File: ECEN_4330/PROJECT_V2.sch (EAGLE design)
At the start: 30 parts, among them IC1 74AS573N

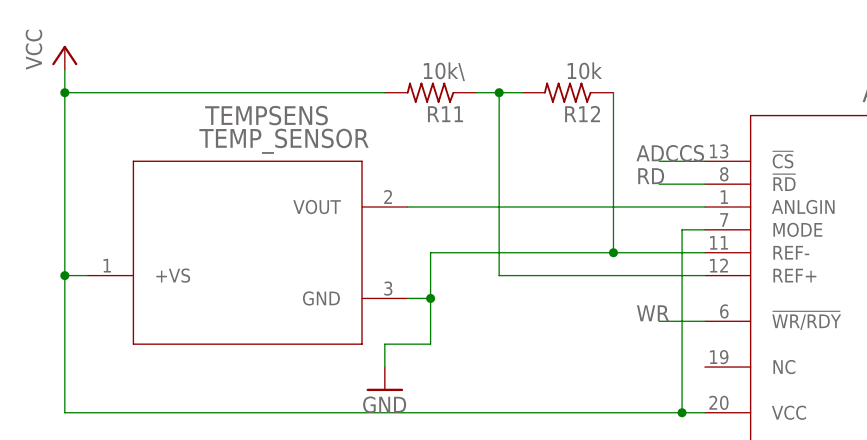
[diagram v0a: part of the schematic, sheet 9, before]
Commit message: Added Color select interfacing
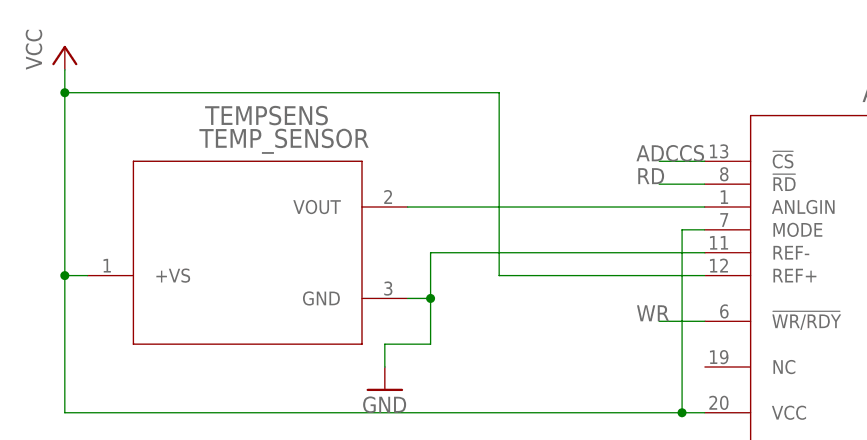
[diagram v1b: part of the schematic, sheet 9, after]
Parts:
- removed R11: 10k\, rcl:R-US_0204/5
- removed R12: 10k, rcl:R-US_0204/5
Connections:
- removed net N$30: ADC.REF+, R11.1, R12.2
- net GND: no longer R12.1
- net P3.5: now also CSLOGICG$1.I6
- net VCC: now also ADC.REF+; no longer R11.2
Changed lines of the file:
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@@
 <part name="GND8" library="supply1" library_urn="urn:adsk.eagle:library:371" deviceset="GND" device=""/>
 <part name="P+10" library="supply1" library_urn="urn:adsk.eagle:library:371" deviceset="VCC" device=""/>
-<part name="R11" library="rcl" library_urn="urn:adsk.eagle:library:334" deviceset="R-US_" device="0204/5" package3d_urn="urn:adsk.eagle:package:23488/1" value="10k\"/>
-<part name="R12" library="rcl" library_urn="urn:adsk.eagle:library:334" deviceset="R-US_" device="0204/5" package3d_urn="urn:adsk.eagle:package:23488/1" value="10k"/>
 <part name="GND9" library="supply1" library_urn="urn:adsk.eagle:library:371" deviceset="GND" device=""/>
 <part name="IC1" library="Fuckboiz" deviceset="74*573" device="N" technology="AS"/>
@@
 </segment>
 </net>
+<net name="COLORCS" class="0">
+<segment>
+<pinref part="CSLOGIC" gate="G$1" pin="O6"/>
+<wire x1="43.18" y1="162.56" x2="48.26" y2="162.56" width="0.1524" layer="91"/>
+<label x="45.72" y="162.56" size="1.778" layer="95"/>
+</segment>
+</net>
 <net name="WR" class="0">
 <segment>
@@
 </segment>
 </net>
-<net name="COLORCS" class="0">
-<segment>
-<pinref part="CSLOGIC" gate="G$1" pin="O6"/>
-<wire x1="43.18" y1="162.56" x2="48.26" y2="162.56" width="0.1524" layer="91"/>
-<label x="45.72" y="162.56" size="1.778" layer="95"/>
+<net name="P3.5" class="0">
+<segment>
+<pinref part="CSLOGIC" gate="G$1" pin="I6"/>
+<wire x1="17.78" y1="154.94" x2="12.7" y2="154.94" width="0.1524" layer="91"/>
+<label x="10.16" y="154.94" size="1.778" layer="95"/>
 </segment>
 </net>
@@
 <instance part="GND8" gate="1" x="132.08" y="106.68"/>
 <instance part="P+10" gate="VCC" x="10.16" y="157.48"/>
-<instance part="R11" gate="G$1" x="50.8" y="152.4" rot="R180"/>
-<instance part="R12" gate="G$1" x="66.04" y="152.4" rot="R180"/>
 <instance part="GND9" gate="1" x="45.72" y="119.38"/>
 </instances>
@@
 <wire x1="50.8" y1="124.46" x2="45.72" y2="124.46" width="0.1524" layer="91"/>
 <pinref part="ADC" gate="A" pin="REF-"/>
-<wire x1="81.28" y1="134.62" x2="71.12" y2="134.62" width="0.1524" layer="91"/>
-<wire x1="71.12" y1="134.62" x2="50.8" y2="134.62" width="0.1524" layer="91"/>
+<wire x1="81.28" y1="134.62" x2="50.8" y2="134.62" width="0.1524" layer="91"/>
 <wire x1="50.8" y1="134.62" x2="50.8" y2="129.54" width="0.1524" layer="91"/>
 <junction x="50.8" y="129.54"/>
-<pinref part="R12" gate="G$1" pin="1"/>
-<wire x1="71.12" y1="152.4" x2="71.12" y2="134.62" width="0.1524" layer="91"/>
-<junction x="71.12" y="134.62"/>
 <pinref part="GND9" gate="1" pin="GND"/>
 <wire x1="45.72" y1="124.46" x2="45.72" y2="121.92" width="0.1524" layer="91"/>
@@
 </segment>
 </net>
-<net name="N$30" class="0">
-<segment>
-<pinref part="R11" gate="G$1" pin="1"/>
-<pinref part="R12" gate="G$1" pin="2"/>
-<wire x1="55.88" y1="152.4" x2="58.42" y2="152.4" width="0.1524" layer="91"/>
-<pinref part="ADC" gate="A" pin="REF+"/>
-<wire x1="58.42" y1="152.4" x2="60.96" y2="152.4" width="0.1524" layer="91"/>
-<wire x1="81.28" y1="132.08" x2="58.42" y2="132.08" width="0.1524" layer="91"/>
-<wire x1="58.42" y1="132.08" x2="58.42" y2="152.4" width="0.1524" layer="91"/>
-<junction x="58.42" y="152.4"/>
-</segment>
-</net>
 <net name="VCC" class="0">
 <segment>
@@
 <wire x1="12.7" y1="132.08" x2="10.16" y2="132.08" width="0.1524" layer="91"/>
 <wire x1="10.16" y1="132.08" x2="10.16" y2="152.4" width="0.1524" layer="91"/>
-<pinref part="R11" gate="G$1" pin="2"/>
-<wire x1="10.16" y1="152.4" x2="45.72" y2="152.4" width="0.1524" layer="91"/>
+<wire x1="10.16" y1="152.4" x2="58.42" y2="152.4" width="0.1524" layer="91"/>
 <wire x1="10.16" y1="152.4" x2="10.16" y2="154.94" width="0.1524" layer="91"/>
 <junction x="10.16" y="152.4"/>
@@
 <wire x1="10.16" y1="116.84" x2="10.16" y2="132.08" width="0.1524" layer="91"/>
 <junction x="10.16" y="132.08"/>
-</segment>
-</net>
+<pinref part="ADC" gate="A" pin="REF+"/>
+<wire x1="81.28" y1="132.08" x2="58.42" y2="132.08" width="0.1524" layer="91"/>
+<wire x1="58.42" y1="132.08" x2="58.42" y2="152.4" width="0.1524" layer="91"/>
+</segment>
+</net>

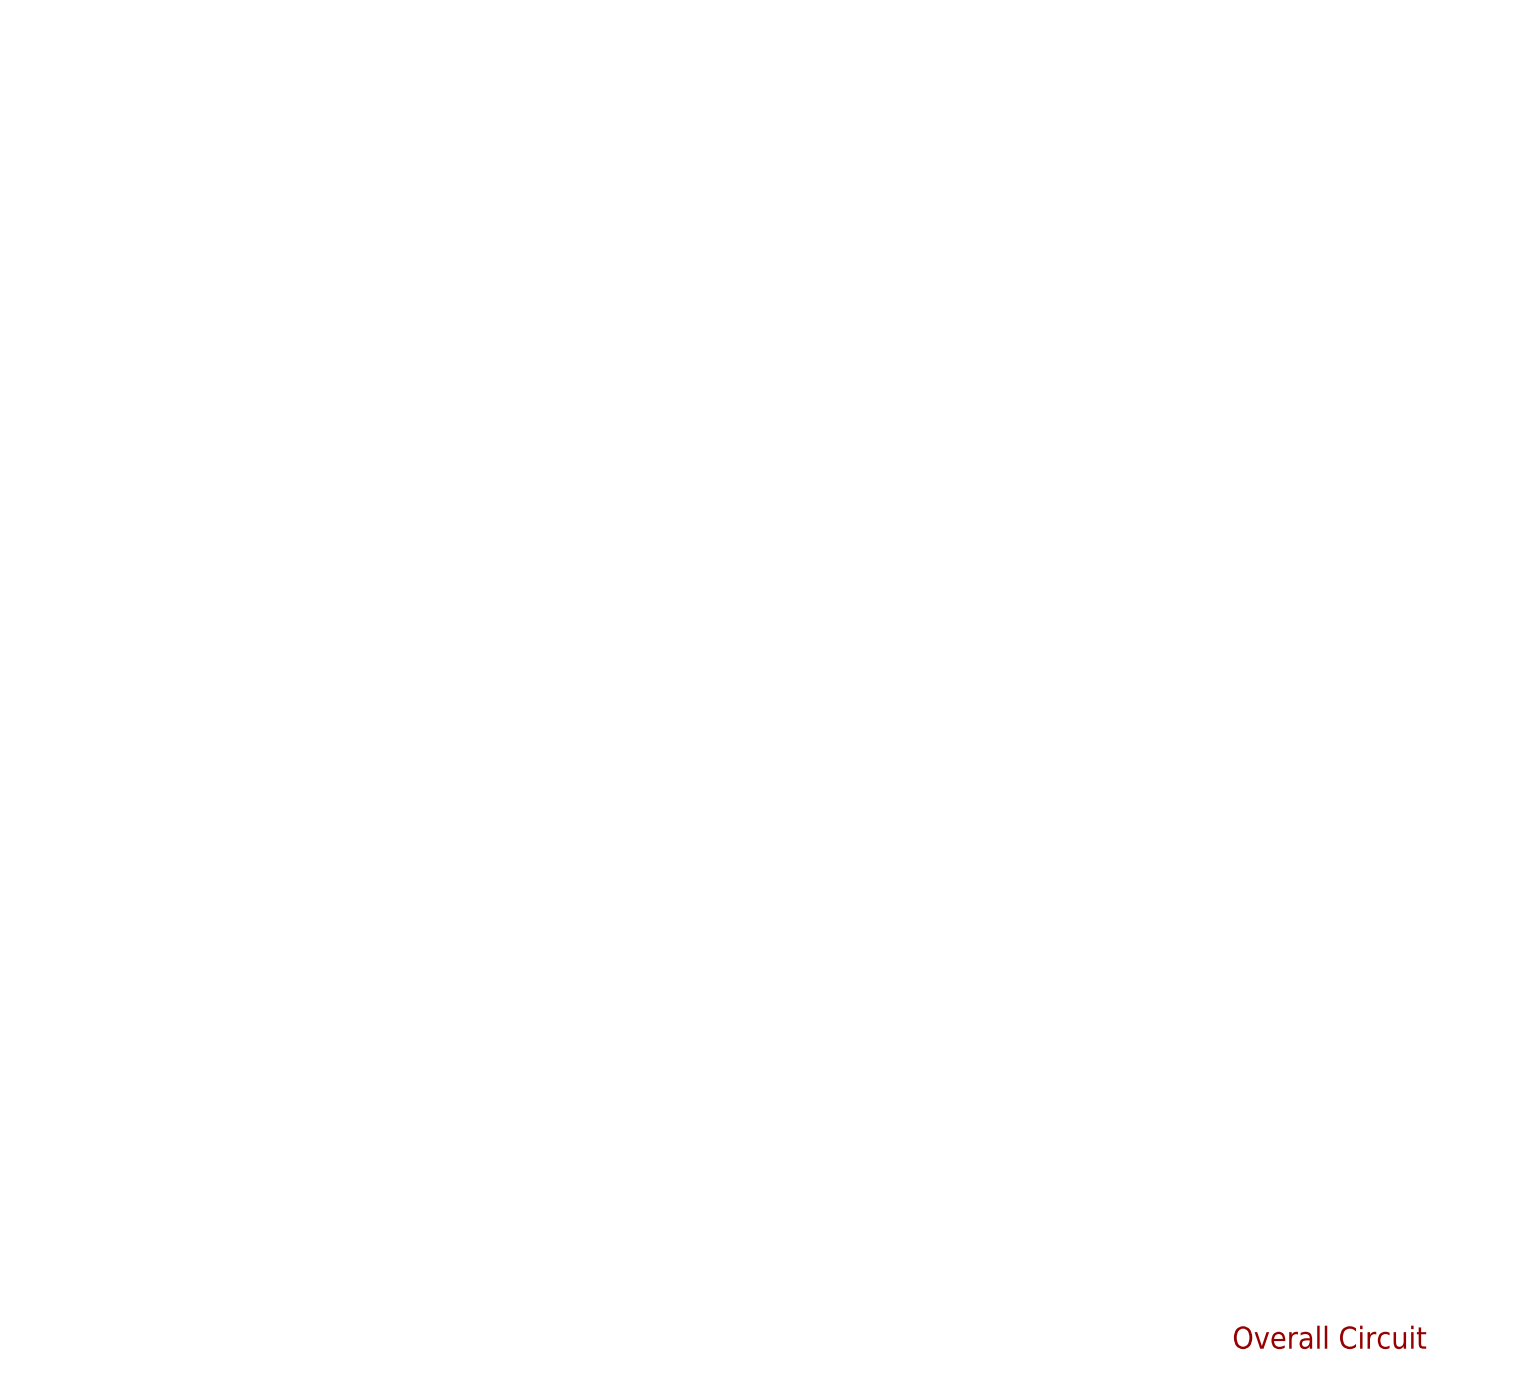
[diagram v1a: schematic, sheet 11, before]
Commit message: Started adding power circuit, changed switch to match footprint, started debugging RTC bug
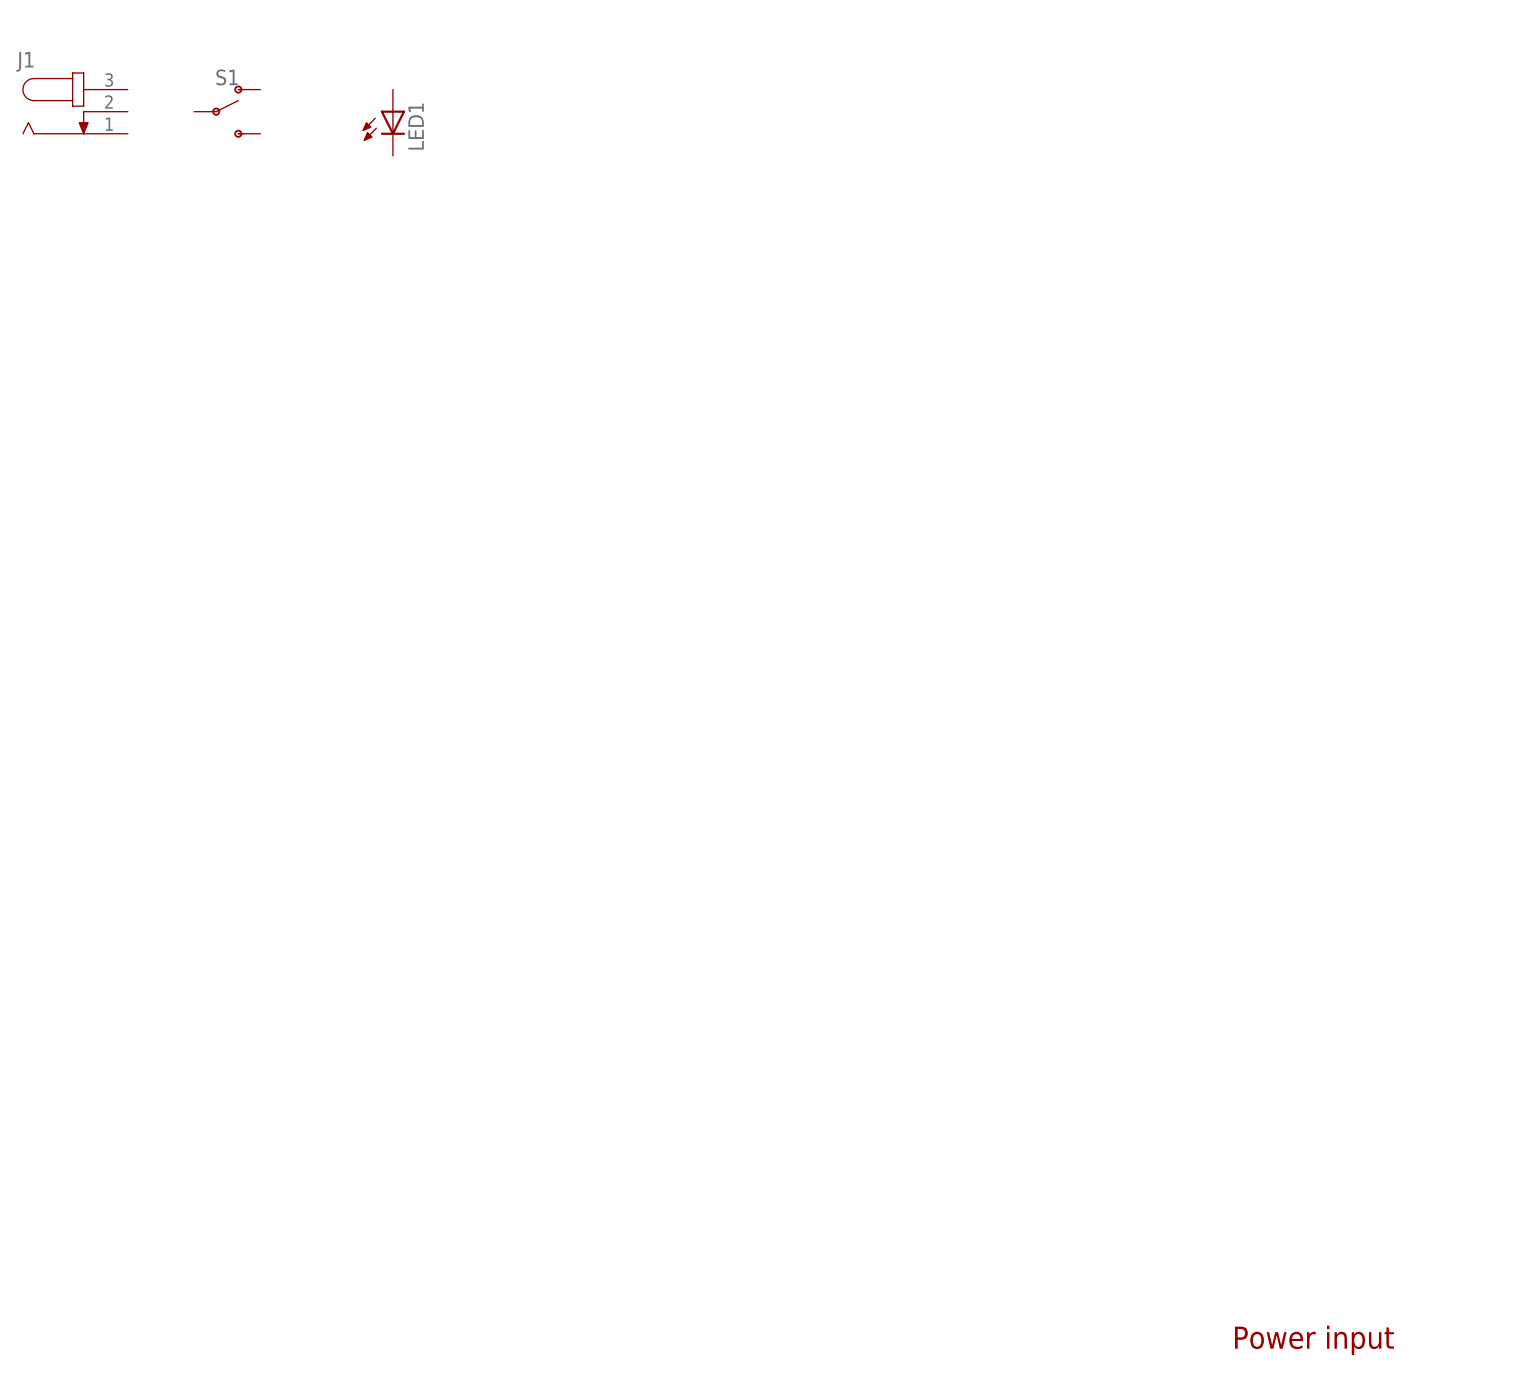
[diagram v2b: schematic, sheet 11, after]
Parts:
- removed RSTSW: (no value), adafruit:SWITCH_PUSHBUTTONEVQ-PE
- added J1: (no value), Fuckboiz:JACK-PLUG0
- added LED1: (no value), adafruit:LED5MM
- added RSTSWITCH: MOMENTARY-SWITCH-SPST-PTH-6.0MM, SparkFun-Switches:MOMENTARY-SWITCH-SPST-PTH-6.0MM
- added S1: (no value), Fuckboiz:SPDT_SWITCH-PTH-11.6X4.0MM-LOCK
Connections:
- net N$15: now also RSTSWITCH.1; no longer RSTSW.P$1
- net VCC: now also RSTSWITCH.2; no longer RSTSW.P$2
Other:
- note added: "Power input"
- note removed: "Overall Circuit"

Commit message: Final design before hierarchiel block
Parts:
- added R11: (no value), resistor:R-US_0204/7
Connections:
- new net N$30: J1.3, LED1.A, S1.S
- new net N$48: S1.O
- new net N$49: LED1.C, R11.2
- net GND: now also J1.1, J1.2, R11.1
- net VCC: now also S1.P
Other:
- moved on the sheet: J1, LED1, RAM1, RAM2, RTC, S1

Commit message: Added hierarchy sheet
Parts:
- removed 7SEG: 7_SEG, Fuckboiz:7_SEG
- removed 7SEGLATCH: 74HC573N, Fuckboiz:74HC573N
- removed ADC: ADC, Fuckboiz:ADC
- removed C1: 10u, adafruit:C-US025-025X050
- removed CLK: (no value), crystal:XO-8
- removed CSLOGIC: (no value), pal:22V10
- removed DEMULTIPLEXER, IC1: 74AS573N, Fuckboiz:74AS573N
- removed J1: (no value), Fuckboiz:JACK-PLUG0
- removed KEYPAD: (no value), Fuckboiz:KEYPAD4X4
- removed LCD: (no value), Fuckboiz:LCD
- removed LED1: (no value), adafruit:LED5MM
- removed MICROCONTROLLER: 8051P, Fuckboiz:8051P
- removed R1: 8.2k, rcl:R-US_0204/5
- removed R10: 3362P-1-103LF_POT, Fuckboiz:3362P-1-103LF_POT
- removed R11: (no value), resistor:R-US_0204/7
- removed R2, R3, R4, R5, R6, R7, R8, R9: 330, adafruit:R-US_0204/7
- removed RAM1, RAM2: RAM_32K_8, Fuckboiz:RAM_32K_8
- removed ROM1, ROM2: EEPROM_32K_8, Fuckboiz:EEPROM_32K_8
- removed RSTSWITCH: MOMENTARY-SWITCH-SPST-PTH-6.0MM, SparkFun-Switches:MOMENTARY-SWITCH-SPST-PTH-6.0MM
- removed RTC: (no value), Fuckboiz:RTC-72421
- removed S1: (no value), Fuckboiz:SPDT_SWITCH-PTH-11.6X4.0MM-LOCK
- removed TEMPSENS: TEMP_SENSOR, Fuckboiz:TEMP_SENSOR
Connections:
- removed net 7SEGCSWR: 7SEGLATCHA.C, CSLOGICG$1.O9
- removed net A0: DEMULTIPLEXERA.8Q, LCD.RS, RAM1.A0, RAM2.A0, ROM1.A0, ROM2.A0
- removed net A1: DEMULTIPLEXERA.7Q, LCD.R/W~, RAM1.A1, RAM2.A1, ROM1.A1, ROM2.A1
- removed net A10: MICROCONTROLLER.P22-A10, RAM1.A10, RAM2.A10, ROM1.A10, ROM2.A10
- removed net A11: MICROCONTROLLER.P23-A11, RAM1.A11, RAM2.A11, ROM1.A11, ROM2.A11
- removed net A12: MICROCONTROLLER.P24-A12, RAM1.A12, RAM2.A12, ROM1.A12, ROM2.A12
- removed net A13: CSLOGICG$1.I3, MICROCONTROLLER.P25-A13, RAM1.A13, RAM2.A13, ROM1.A13, ROM2.A13
- removed net A14: CSLOGICG$1.I2, MICROCONTROLLER.P26-A14, RAM1.A14, RAM2.A14, ROM1.A14, ROM2.A14
- removed net A15: CSLOGICG$1.I1, MICROCONTROLLER.P27-A15
- removed net A2: DEMULTIPLEXERA.6Q, RAM1.A2, RAM2.A2, ROM1.A2, ROM2.A2
- removed net A3: DEMULTIPLEXERA.5Q, RAM1.A3, RAM2.A3, ROM1.A3, ROM2.A3
- removed net A4: DEMULTIPLEXERA.4Q, RAM1.A4, RAM2.A4, ROM1.A4, ROM2.A4
- removed net A5: DEMULTIPLEXERA.3Q, RAM1.A5, RAM2.A5, ROM1.A5, ROM2.A5
- removed net A6: DEMULTIPLEXERA.2Q, RAM1.A6, RAM2.A6, ROM1.A6, ROM2.A6
- removed net A7: DEMULTIPLEXERA.1Q, RAM1.A7, RAM2.A7, ROM1.A7, ROM2.A7
- removed net A8: MICROCONTROLLER.P20-A8, RAM1.A8, RAM2.A8, ROM1.A8, ROM2.A8
- removed net A9: MICROCONTROLLER.P21-A9, RAM1.A9, RAM2.A9, ROM1.A9, ROM2.A9
- removed net ADCCS: ADC.!CS, CSLOGICG$1.O0
- removed net ALE: RTC.3
- removed net COLORCS: CSLOGICG$1.O6, IC1A.C
- removed net D0: 7SEGLATCHA.1D, DEMULTIPLEXERA.1D, IC1A.1D, LCD.DB0, MICROCONTROLLER.P00-AD0, RAM1.I/O0, RAM2.I/O0, ROM1.I/O0, ROM2.I/O0, RTC.14, RTC.4
- removed net D1: 7SEGLATCHA.2D, ADC.D0, ADC.D1, DEMULTIPLEXERA.2D, IC1A.2D, LCD.DB1, MICROCONTROLLER.P01-AD1, RAM1.I/O1, RAM2.I/O1, ROM1.I/O1, ROM2.I/O1, RTC.13, RTC.5
- removed net D2: 7SEGLATCHA.3D, ADC.D2, DEMULTIPLEXERA.3D, IC1A.3D, LCD.DB2, MICROCONTROLLER.P02-AD2, RAM1.I/O2, RAM2.I/O2, ROM1.I/O2, ROM2.I/O2, RTC.12, RTC.6
- removed net D3: 7SEGLATCHA.4D, ADC.D3, DEMULTIPLEXERA.4D, LCD.DB3, MICROCONTROLLER.P03-AD3, RAM1.I/O3, RAM2.I/O3, ROM1.I/O3, ROM2.I/O3, RTC.11, RTC.7
- removed net D4: 7SEGLATCHA.5D, ADC.D4, DEMULTIPLEXERA.5D, LCD.DB4, MICROCONTROLLER.P04-AD4, RAM1.I/O4, RAM2.I/O4, ROM1.I/O4, ROM2.I/O4
- removed net D5: 7SEGLATCHA.6D, ADC.D5, DEMULTIPLEXERA.6D, LCD.DB5, MICROCONTROLLER.P05-AD5, RAM1.I/O5, RAM2.I/O5, ROM1.I/O5, ROM2.I/O5
- removed net D6: 7SEGLATCHA.7D, ADC.D6, DEMULTIPLEXERA.7D, LCD.DB6, MICROCONTROLLER.P06-AD6, RAM1.I/O6, RAM2.I/O6, ROM1.I/O6, ROM2.I/O6
- removed net D7: 7SEGLATCHA.8D, ADC.D7, DEMULTIPLEXERA.8D, LCD.DB7, MICROCONTROLLER.P07-AD7, RAM1.I/O7, RAM2.I/O7, ROM1.I/O7, ROM2.I/O7
- removed net GND: 7SEGLATCHA.OC, ADC.GND, ADC.REF-, CLK.GND, DEMULTIPLEXERA.OC, IC1A.OC, J1.1, J1.2, LCD.VSS, MICROCONTROLLER.EA, MICROCONTROLLER.GND, R1.1, R10.1, R11.1, RAM1.GND, RAM2.GND, ROM1.GND, ROM2.GND, RTC.9, TEMPSENS.GND
- removed net LCDCS: CSLOGICG$1.O7, LCD.EN
- removed net N$1: RTC.1
- removed net N$10: 7SEG.G, R8.2
- removed net N$11: 7SEG.F, R7.2
- removed net N$12: 7SEG.E, R6.2
- removed net N$13: 7SEG.D, R5.2
- removed net N$14: 7SEG.C, R4.2
- removed net N$15: C1.2, MICROCONTROLLER.RST, R1.2, RSTSWITCH.1
- removed net N$16: LCD.VO, R10.2
- removed net N$17: IC1A.1Q, LCD.R
- removed net N$18: MICROCONTROLLER.P30-RXD
- removed net N$19: MICROCONTROLLER.P31-TXD
- removed net N$2: DEMULTIPLEXERA.C, MICROCONTROLLER.ALE
- removed net N$20: MICROCONTROLLER.P32-INT0
- removed net N$21: MICROCONTROLLER.P33-INT1
- removed net N$22: MICROCONTROLLER.P34-T0
- removed net N$23: IC1A.2Q, LCD.G
- removed net N$24: IC1A.3Q, LCD.B
- removed net N$25: RTC.16
- removed net N$26: ADC.ANLGIN, TEMPSENS.VOUT
- removed net N$27: ADC.!INT
- removed net N$28: ADC.!OFLW
- removed net N$29: RTC.17
- removed net N$3: 7SEGLATCHA.1Q, R2.1
- removed net N$30: J1.3, LED1.A, S1.S
- removed net N$31: MICROCONTROLLER.XTAL2
- removed net N$32: IC1A.4D
- removed net N$33: 7SEG.B, R3.2
- removed net N$34: IC1A.5D
- removed net N$35: CSLOGICG$1.CLK/I0
- removed net N$36: IC1A.6D
- removed net N$37: IC1A.7D
- removed net N$38: IC1A.8D
- removed net N$39: IC1A.4Q
- removed net N$4: 7SEGLATCHA.2Q, R3.1
- removed net N$40: IC1A.5Q
- removed net N$41: IC1A.6Q
- removed net N$42: IC1A.7Q
- removed net N$43: 7SEG.A, R2.2
- removed net N$44: 7SEG.DP, R9.2
- removed net N$45: 7SEGLATCHA.8Q, R9.1
- removed net N$46: IC1A.8Q
- removed net N$48: S1.O
- removed net N$49: LED1.C, R11.2
- removed net N$5: 7SEGLATCHA.3Q, R4.1
- removed net N$6: 7SEGLATCHA.4Q, R5.1
- removed net N$7: 7SEGLATCHA.5Q, R6.1
- removed net N$8: 7SEGLATCHA.6Q, R7.1
- removed net N$9: 7SEGLATCHA.7Q, R8.1
- removed net NC: ROM1.!WE, ROM2.!WE
- removed net P1.0: KEYPAD.C1, MICROCONTROLLER.P10-T2
- removed net P1.1: KEYPAD.C2, MICROCONTROLLER.P11-T2EX
- removed net P1.2: KEYPAD.C3, MICROCONTROLLER.P12
- removed net P1.3: KEYPAD.C4, MICROCONTROLLER.P13
- removed net P1.4: KEYPAD.R1, MICROCONTROLLER.P14
- removed net P1.5: KEYPAD.R2, MICROCONTROLLER.P15
- removed net P1.6: KEYPAD.R3, MICROCONTROLLER.P16
- removed net P1.7: KEYPAD.R4, MICROCONTROLLER.P17
- removed net P3.5: CSLOGICG$1.I6, MICROCONTROLLER.P35-T1
- removed net PSEN: CSLOGICG$1.I0, MICROCONTROLLER.PSEN
- removed net RAM1CS: CSLOGICG$1.O2, RAM1.!CE
- removed net RAM2CS: CSLOGICG$1.O1, RAM2.!CE
- removed net RD: ADC.!RD, CSLOGICG$1.I5, MICROCONTROLLER.P37-RD, RAM1.!OE, RAM2.!OE, RTC.8
- removed net ROM1CS: CSLOGICG$1.O4, ROM1.!CE, ROM1.!OE
- removed net ROM2CS: CSLOGICG$1.O3, ROM2.!CE, ROM2.!OE
- removed net RTCCS: CSLOGICG$1.O8, RTC.2
- removed net VCC: 7SEG.CA, 7SEG.CA@1, ADC.MODE, ADC.REF+, ADC.VCC, C1.1, CLK.VCC, LCD.BL, LCD.VDD, MICROCONTROLLER.VCC, R10.3, RAM1.VCC, RAM2.VCC, ROM1.VCC, ROM2.VCC, RSTSWITCH.2, RTC.15, RTC.18, S1.P, TEMPSENS.+VS
- removed net WR: ADC.!WR/RDY, CSLOGICG$1.I4, MICROCONTROLLER.P36-WR, RAM1.!WE, RAM2.!WE, RTC.10
- removed net XTAL1: CLK.OUT, MICROCONTROLLER.XTAL1
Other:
- note added: "Justin Pachl ECEN 4330 OVERALL SCHEMATIC"

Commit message: Started board, fixed ERC issues
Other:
- note removed: "Latch?"
